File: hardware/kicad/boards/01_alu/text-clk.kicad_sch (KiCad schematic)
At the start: 8 parts, among them U10701 ICM7555xB, U10702 74HCT541

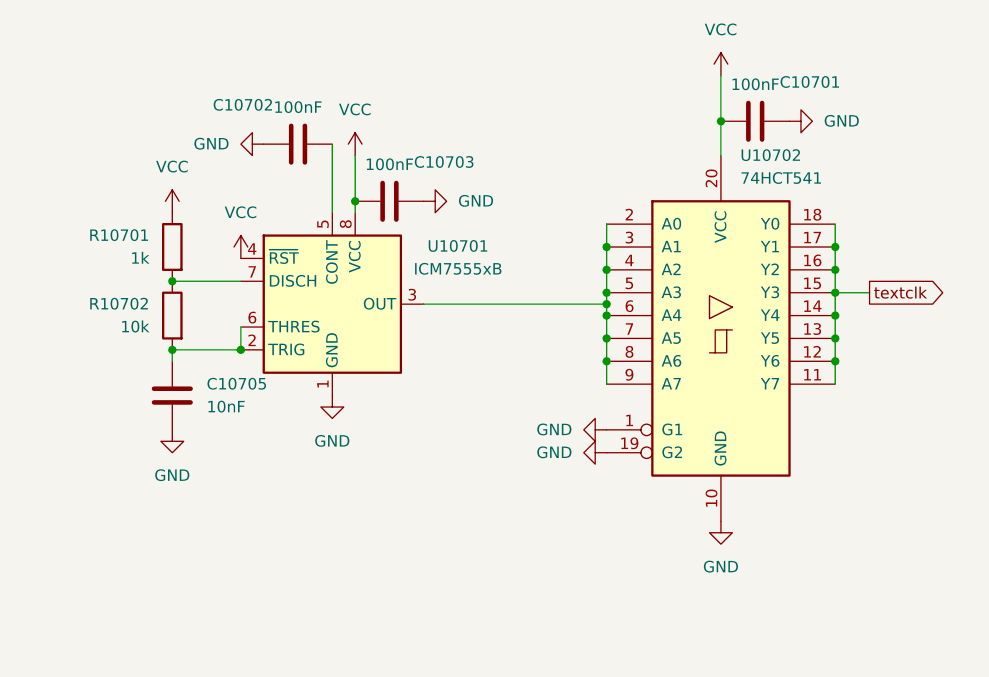
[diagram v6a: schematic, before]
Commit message: arch: added LEDs, override switches; fixed errors and warnings to 0
ready for routing after logical coherence check
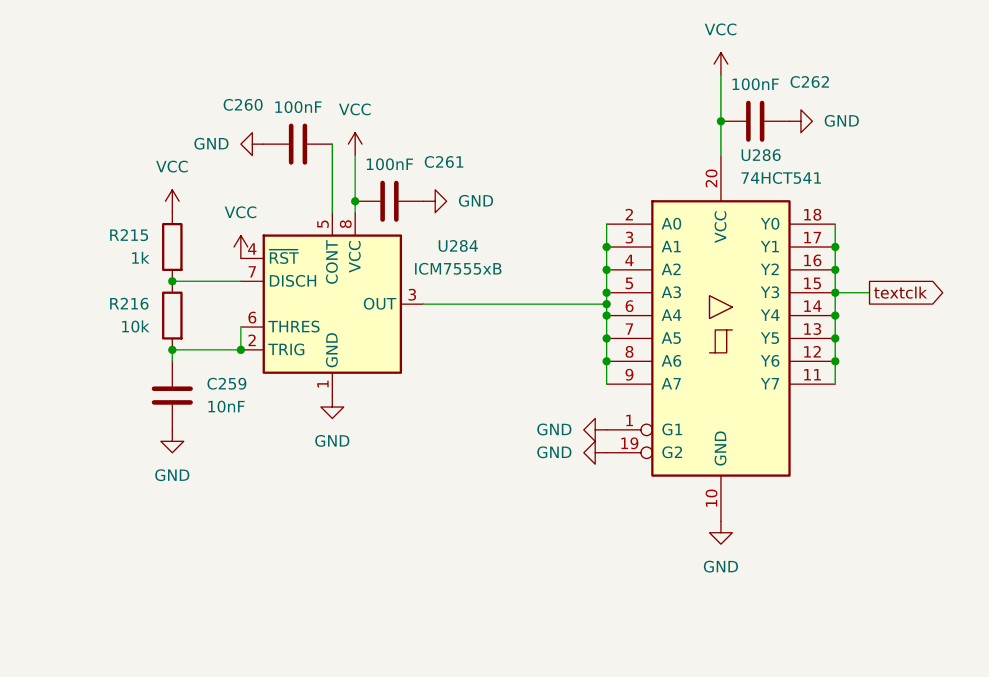
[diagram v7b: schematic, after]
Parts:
- renumbered C10705 to C259, C10702 to C260, C10703 to C261, C10701 to C262, R10701 to R215, R10702 to R216, U10701 to U284, U10702 to U286
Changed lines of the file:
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@@
 		(dnp no)
 		(fields_autoplaced yes)
-		(property "Reference" "#PWR010706"
+		(property "Reference" "#PWR01044"
 			(at 110.49 53.34 0)
 			(hide yes)
@@
 			(project "alu-32b"
 				(path "/ddad1417-0afc-402d-a021-92fc87ddd78a/70179ff6-7c16-4036-adf3-4ea9b5e0a238/259ce3bc-a28b-4687-b086-c0ff5aa711b4"
-					(reference "#PWR010706")
+					(reference "#PWR01044")
 					(unit 1)
 				)
@@
 		(dnp no)
 		(fields_autoplaced yes)
-		(property "Reference" "U10702"
+		(property "Reference" "U286"
 			(at 173.5933 43.18 0)
 			(show_name no)
@@
 			(project "alu-32b"
 				(path "/ddad1417-0afc-402d-a021-92fc87ddd78a/70179ff6-7c16-4036-adf3-4ea9b5e0a238/259ce3bc-a28b-4687-b086-c0ff5aa711b4"
-					(reference "U10702")
+					(reference "U286")
 					(unit 1)
 				)
@@
 		(dnp no)
 		(fields_autoplaced yes)
-		(property "Reference" "#PWR010703"
+		(property "Reference" "#PWR01047"
 			(at 114.3 41.91 0)
 			(hide yes)
@@
 			(project "alu-32b"
 				(path "/ddad1417-0afc-402d-a021-92fc87ddd78a/70179ff6-7c16-4036-adf3-4ea9b5e0a238/259ce3bc-a28b-4687-b086-c0ff5aa711b4"
-					(reference "#PWR010703")
+					(reference "#PWR01047")
 					(unit 1)
 				)
@@
 		(in_pos_files yes)
 		(dnp no)
-		(property "Reference" "C10702"
+		(property "Reference" "C260"
 			(at 118.364 37.592 90)
 			(show_name no)
@@
 			(project "alu-32b"
 				(path "/ddad1417-0afc-402d-a021-92fc87ddd78a/70179ff6-7c16-4036-adf3-4ea9b5e0a238/259ce3bc-a28b-4687-b086-c0ff5aa711b4"
-					(reference "C10702")
+					(reference "C260")
 					(unit 1)
 				)
@@
 		(in_pos_files yes)
 		(dnp no)
-		(property "Reference" "R10701"
+		(property "Reference" "R215"
 			(at 107.95 52.0699 0)
 			(show_name no)
@@
 			(project "alu-32b"
 				(path "/ddad1417-0afc-402d-a021-92fc87ddd78a/70179ff6-7c16-4036-adf3-4ea9b5e0a238/259ce3bc-a28b-4687-b086-c0ff5aa711b4"
-					(reference "R10701")
+					(reference "R215")
 					(unit 1)
 				)
@@
 		(dnp no)
 		(fields_autoplaced yes)
-		(property "Reference" "U10701"
+		(property "Reference" "U284"
 			(at 142.24 53.2698 0)
 			(show_name no)
@@
 			(project "alu-32b"
 				(path "/ddad1417-0afc-402d-a021-92fc87ddd78a/70179ff6-7c16-4036-adf3-4ea9b5e0a238/259ce3bc-a28b-4687-b086-c0ff5aa711b4"
-					(reference "U10701")
+					(reference "U284")
 					(unit 1)
 				)
@@
 		(dnp no)
 		(fields_autoplaced yes)
-		(property "Reference" "#PWR010710"
+		(property "Reference" "#PWR01048"
 			(at 128.27 76.2 0)
 			(hide yes)
@@
 			(project "alu-32b"
 				(path "/ddad1417-0afc-402d-a021-92fc87ddd78a/70179ff6-7c16-4036-adf3-4ea9b5e0a238/259ce3bc-a28b-4687-b086-c0ff5aa711b4"
-					(reference "#PWR010710")
+					(reference "#PWR01048")
 					(unit 1)
 				)
@@
 		(in_pos_files yes)
 		(dnp no)
-		(property "Reference" "C10701"
+		(property "Reference" "C262"
 			(at 181.356 35.052 90)
 			(show_name no)
@@
 			(project "alu-32b"
 				(path "/ddad1417-0afc-402d-a021-92fc87ddd78a/70179ff6-7c16-4036-adf3-4ea9b5e0a238/259ce3bc-a28b-4687-b086-c0ff5aa711b4"
-					(reference "C10701")
+					(reference "C262")
 					(unit 1)
 				)
@@
 		(in_pos_files yes)
 		(dnp no)
-		(property "Reference" "R10702"
+		(property "Reference" "R216"
 			(at 107.95 59.6899 0)
 			(show_name no)
@@
 			(project "alu-32b"
 				(path "/ddad1417-0afc-402d-a021-92fc87ddd78a/70179ff6-7c16-4036-adf3-4ea9b5e0a238/259ce3bc-a28b-4687-b086-c0ff5aa711b4"
-					(reference "R10702")
+					(reference "R216")
 					(unit 1)
 				)
@@
 		(dnp no)
 		(fields_autoplaced yes)
-		(property "Reference" "#PWR010707"
+		(property "Reference" "#PWR01046"
 			(at 118.11 58.42 0)
 			(hide yes)
@@
 			(project "alu-32b"
 				(path "/ddad1417-0afc-402d-a021-92fc87ddd78a/70179ff6-7c16-4036-adf3-4ea9b5e0a238/259ce3bc-a28b-4687-b086-c0ff5aa711b4"
-					(reference "#PWR010707")
+					(reference "#PWR01046")
 					(unit 1)
 				)
@@
 		(dnp no)
 		(fields_autoplaced yes)
-		(property "Reference" "#PWR010714"
+		(property "Reference" "#PWR01056"
 			(at 171.45 90.17 0)
 			(hide yes)
@@
 			(project "alu-32b"
 				(path "/ddad1417-0afc-402d-a021-92fc87ddd78a/70179ff6-7c16-4036-adf3-4ea9b5e0a238/259ce3bc-a28b-4687-b086-c0ff5aa711b4"
-					(reference "#PWR010714")
+					(reference "#PWR01056")
 					(unit 1)
 				)
@@
 		(dnp no)
 		(fields_autoplaced yes)
-		(property "Reference" "#PWR010713"
+		(property "Reference" "#PWR01054"
 			(at 152.4 76.2 0)
 			(hide yes)
@@
 			(project "alu-32b"
 				(path "/ddad1417-0afc-402d-a021-92fc87ddd78a/70179ff6-7c16-4036-adf3-4ea9b5e0a238/259ce3bc-a28b-4687-b086-c0ff5aa711b4"
-					(reference "#PWR010713")
+					(reference "#PWR01054")
 					(unit 1)
 				)
@@
 		(dnp no)
 		(fields_autoplaced yes)
-		(property "Reference" "#PWR010701"
+		(property "Reference" "#PWR01055"
 			(at 171.45 38.1 0)
 			(hide yes)
@@
 			(project "alu-32b"
 				(path "/ddad1417-0afc-402d-a021-92fc87ddd78a/70179ff6-7c16-4036-adf3-4ea9b5e0a238/259ce3bc-a28b-4687-b086-c0ff5aa711b4"
-					(reference "#PWR010701")
+					(reference "#PWR01055")
 					(unit 1)
 				)
@@
 		(dnp no)
 		(fields_autoplaced yes)
-		(property "Reference" "#PWR010705"
+		(property "Reference" "#PWR01050"
 			(at 144.78 48.26 0)
 			(hide yes)
@@
 			(project "alu-32b"
 				(path "/ddad1417-0afc-402d-a021-92fc87ddd78a/70179ff6-7c16-4036-adf3-4ea9b5e0a238/259ce3bc-a28b-4687-b086-c0ff5aa711b4"
-					(reference "#PWR010705")
+					(reference "#PWR01050")
 					(unit 1)
 				)
@@
 		(dnp no)
 		(fields_autoplaced yes)
-		(property "Reference" "#PWR010704"
+		(property "Reference" "#PWR01049"
 			(at 130.81 46.99 0)
 			(hide yes)
@@
 			(project "alu-32b"
 				(path "/ddad1417-0afc-402d-a021-92fc87ddd78a/70179ff6-7c16-4036-adf3-4ea9b5e0a238/259ce3bc-a28b-4687-b086-c0ff5aa711b4"
-					(reference "#PWR010704")
+					(reference "#PWR01049")
 					(unit 1)
 				)
@@
 		(dnp no)
 		(fields_autoplaced yes)
-		(property "Reference" "#PWR010712"
+		(property "Reference" "#PWR01053"
 			(at 152.4 73.66 0)
 			(hide yes)
@@
 			(project "alu-32b"
 				(path "/ddad1417-0afc-402d-a021-92fc87ddd78a/70179ff6-7c16-4036-adf3-4ea9b5e0a238/259ce3bc-a28b-4687-b086-c0ff5aa711b4"
-					(reference "#PWR010712")
+					(reference "#PWR01053")
 					(unit 1)
 				)
@@
 		(dnp no)
 		(fields_autoplaced yes)
-		(property "Reference" "#PWR010702"
+		(property "Reference" "#PWR01057"
 			(at 185.42 39.37 0)
 			(hide yes)
@@
 			(project "alu-32b"
 				(path "/ddad1417-0afc-402d-a021-92fc87ddd78a/70179ff6-7c16-4036-adf3-4ea9b5e0a238/259ce3bc-a28b-4687-b086-c0ff5aa711b4"
-					(reference "#PWR010702")
+					(reference "#PWR01057")
 					(unit 1)
 				)
@@
 		(dnp no)
 		(fields_autoplaced yes)
-		(property "Reference" "C10705"
+		(property "Reference" "C259"
 			(at 114.3 68.5799 0)
 			(show_name no)
@@
 			(project "alu-32b"
 				(path "/ddad1417-0afc-402d-a021-92fc87ddd78a/70179ff6-7c16-4036-adf3-4ea9b5e0a238/259ce3bc-a28b-4687-b086-c0ff5aa711b4"
-					(reference "C10705")
+					(reference "C259")
 					(unit 1)
 				)
@@
 		(in_pos_files yes)
 		(dnp no)
-		(property "Reference" "C10703"
+		(property "Reference" "C261"
 			(at 140.716 43.942 90)
 			(show_name no)
@@
 			(project "alu-32b"
 				(path "/ddad1417-0afc-402d-a021-92fc87ddd78a/70179ff6-7c16-4036-adf3-4ea9b5e0a238/259ce3bc-a28b-4687-b086-c0ff5aa711b4"
-					(reference "C10703")
+					(reference "C261")
 					(unit 1)
 				)
@@
 		(dnp no)
 		(fields_autoplaced yes)
-		(property "Reference" "#PWR010711"
+		(property "Reference" "#PWR01045"
 			(at 110.49 80.01 0)
 			(hide yes)
@@
 			(project "alu-32b"
 				(path "/ddad1417-0afc-402d-a021-92fc87ddd78a/70179ff6-7c16-4036-adf3-4ea9b5e0a238/259ce3bc-a28b-4687-b086-c0ff5aa711b4"
-					(reference "#PWR010711")
-					(unit 1)
-				)
+					(reference "#PWR01045")
+					(unit 1)
+				)

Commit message: chore: cleanup and annotation  of alu subboards; hygiene before routing
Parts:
- removed C262: 100nF, Capacitor_SMD:C_0805_2012Metric, symbol Device:C
- removed U286: 74HCT541, Package_SO:SOIC-20W_7.5x12.8mm_P1.27mm, symbol 74xx:74HCT541
- renumbered C259 to C258, C260 to C259, C261 to C260, R215 to R175, R216 to R176, U284 to U278
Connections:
- net textclk: now also U278.3 (OUT)
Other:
- moved on the sheet: C258, C259, C260, R175, R176, U278
